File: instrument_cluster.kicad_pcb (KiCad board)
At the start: 2 copper layers, 144.8 x 45.7 mm, 76 parts, among them J1 Conn_02x16_Top_Bottom, J2 Conn_02x16_Top_Bottom, J3 USB mini-B SMD, J4 NOT_FITTED_SWD_Conn_01x04_Male, J5 54819-0572, J6 NOT_FITTED_SWD_Conn_01x04_Male, U1 LM2575S-5.0_NOPB, U10 74HC4050D, U11 TJA1040T, U12 TJA1040T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

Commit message: working with pcb design
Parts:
- D3, D5, D6: moved to B.Cu
- moved R18 98.0 mm to (150.5, 145.5)
- moved C29 97.7 mm to (146.0, 145.5)
- moved C28 97.5 mm to (142.0, 145.5)
- moved R17 97.4 mm to (154.0, 144.5)
- moved R20 94.6 mm to (154.9, 141.5), turned to 180 degrees
- moved R21 94.1 mm to (151.5, 141.5), turned to 180 degrees
- moved R22 93.2 mm to (146.5, 141.0), turned to 180 degrees
- moved R23 93.0 mm to (142.9, 141.0), turned to 180 degrees
- moved C5 87.6 mm to (151.0, 127.5), turned to 180 degrees
- moved U12 82.4 mm to (144.5, 135.5), turned to 90 degrees
- moved U11 82.0 mm to (153.5, 136.0), turned to 90 degrees
- moved C7 79.0 mm to (143.0, 127.0), turned to 270 degrees
- moved D6 78.9 mm to (168.0, 122.0), turned to 270 degrees
- moved C6 61.6 mm to (149.0, 100.0), turned to 180 degrees
- moved C8 47.1 mm to (143.0, 95.0)
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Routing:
- net GND: track 159.1 -> 287.4 mm, vias 2 -> 9
- net /MS_CAN_H: track 34.8 -> 145.8 mm
- net /MS_CAN_L: track 40.4 -> 148.0 mm
- net /HS_CAN_H: track 31.1 -> 138.4 mm, vias 0 -> 1
- net /HS_CAN_L: track 32.4 -> 137.2 mm, vias 0 -> 1
- net /+5V_B: track 0.00 -> 52.2 mm, vias 0 -> 3
- net /Module B (2can_filter+extra)/anti-theft_stm: track 4.32 -> 52.4 mm, vias 0 -> 2
- net /Module B (2can_filter+extra)/washer: track 4.41 -> 52.2 mm
- net /Module B (2can_filter+extra)/oil_pressure_level: track 7.69 -> 55.1 mm
- net /Module B (2can_filter+extra)/belt: track 10.9 -> 57.8 mm, vias 0 -> 2
- net /Module B (2can_filter+extra)/brake_fluid_level: track 4.07 -> 50.6 mm, vias 0 -> 2
- net /Module B (2can_filter+extra)/trip_comp: track 9.53 -> 55.9 mm, vias 0 -> 2
- net /Module B (2can_filter+extra)/engine_coolant: track 10.5 -> 55.2 mm
- net /Module B (2can_filter+extra)/parking_brakes: track 9.51 -> 53.9 mm, vias 0 -> 2
- net /Module B (2can_filter+extra)/pad_wear: track 4.31 -> 47.8 mm, vias 0 -> 2
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
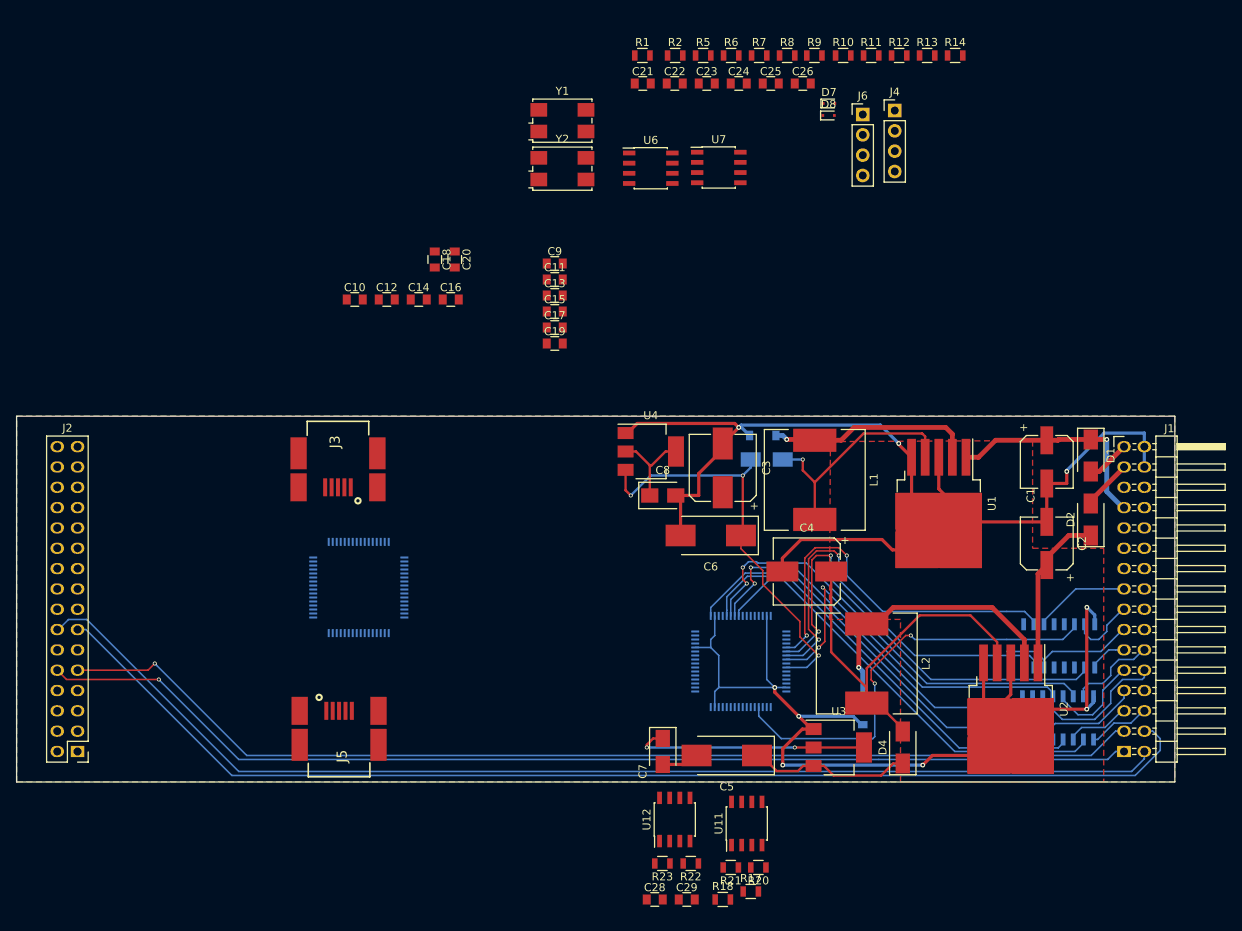
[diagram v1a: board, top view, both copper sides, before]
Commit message: redone shematic of power supply, fix usb_vbus and swd diods connections, change mcu capacitors connections
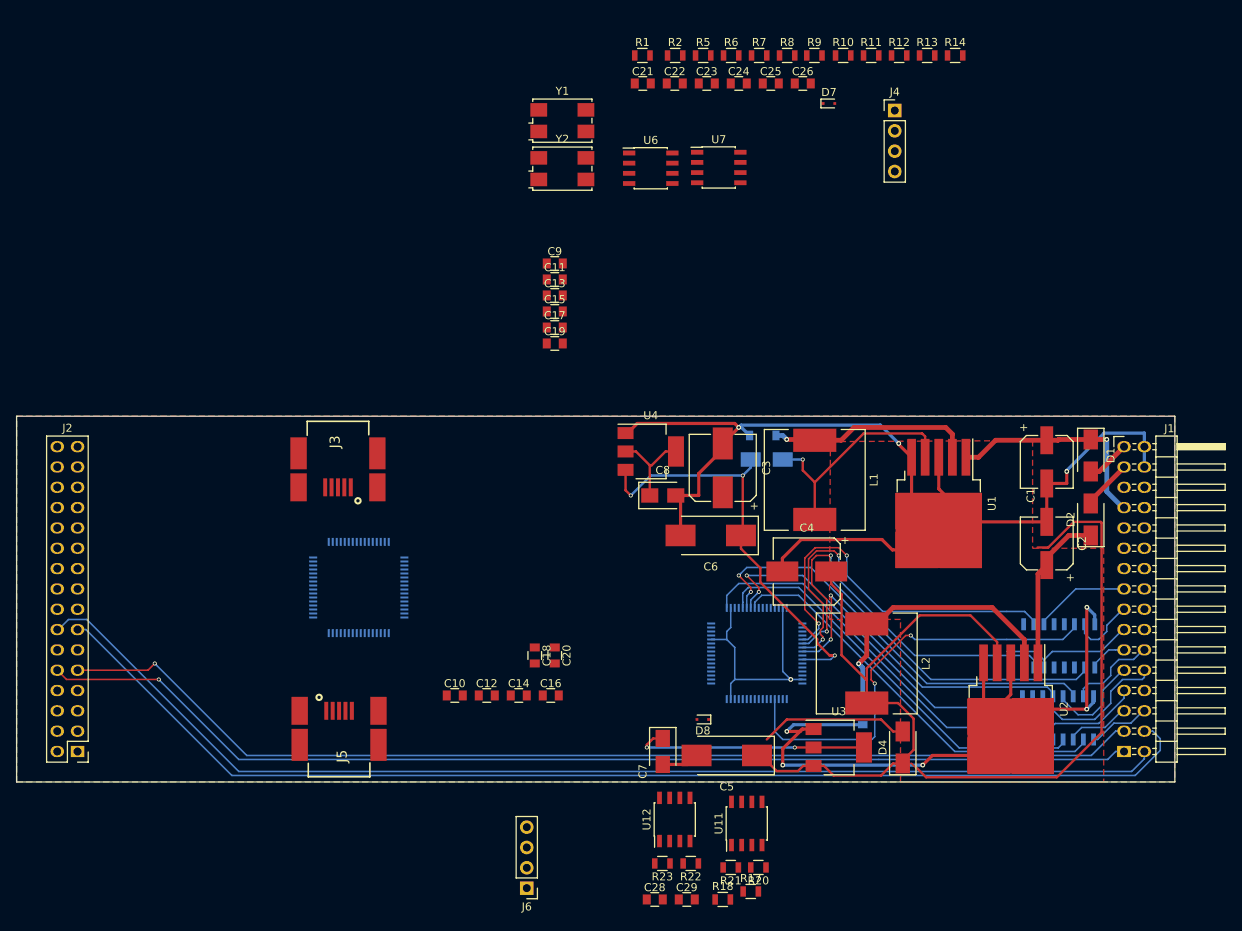
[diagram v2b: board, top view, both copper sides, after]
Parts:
- moved J6 105.4 mm to (126.0, 144.1), turned to 180 degrees
- moved D8 77.1 mm to (148.0, 123.0), turned to 180 degrees
- moved C10 51.1 mm to (117.0, 120.0)
- moved C12 51.1 mm to (121.0, 120.0)
- moved C14 51.1 mm to (125.0, 120.0)
- moved C16 51.1 mm to (129.0, 120.0)
- moved C18 51.1 mm to (127.0, 115.0)
- moved C20 51.1 mm to (129.5, 115.0)
- moved U9 2.24 mm to (154.8, 114.8)
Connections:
- net Net-(J4-Pad2) renamed /Module A (2can_filter)/SWCLK
- net Net-(J4-Pad3) renamed /Module A (2can_filter)/SWDIO
- net Net-(J6-Pad2) renamed /Module B (2can_filter+extra)/SWCLK
- net Net-(J6-Pad3) renamed /Module B (2can_filter+extra)/SWDIO
- C10 pad 1: /+3V3_B -> /+3V3_STM-B
- C11 pad 1: /+3V3_A -> /+3V3_STM-A
- C12 pad 1: /+3V3_B -> /+3V3_STM-B
- C13 pad 1: /+3V3_A -> /+3V3_STM-A
- C14 pad 1: /+3V3_B -> /+3V3_STM-B
- C15 pad 1: /+3V3_A -> /+3V3_STM-A
- C16 pad 1: /+3V3_B -> /+3V3_STM-B
- C17 pad 1: /+3V3_A -> /+3V3_STM-A
- C18 pad 1: /+3V3_B -> /+3V3_STM-B
- C19 pad 1: /+3V3_A -> /+3V3_STM-A
- C20 pad 1: /+3V3_B -> /+3V3_STM-B
- C3 pad 1: /power_supply/+5V_B_module -> /+5V_CAN-B
- C4 pad 1: /power_supply/+5V_A_module -> /+5V_CAN-A
- C5 pad 1: /+5V_A -> /+5V_CAN-A
- C6 pad 1: /+5V_B -> /+5V_CAN-B
- C7 pad 1: /+3V3_A -> Net-(C7-Pad1)
- C8 pad 1: /+3V3_B -> /+3V3_LSH-B
- C9 pad 1: /+3V3_A -> /+3V3_STM-A
- D3 pad 1: /+5V_B -> /+5V_CAN-B
- D3 pad 2: /power_supply/+5V_B_module -> /USB_Vbus-B
- D4 pad 1: /+5V_A -> /+5V_CAN-A
- D4 pad 2: /power_supply/+5V_A_module -> /USB_Vbus-A
- D7 pad 1: /+3V3_A -> /+3V3_STM-A
- D7 pad 2: /+3V3_A -> Net-(C7-Pad1)
- D8 pad 1: /+3V3_B -> /+3V3_STM-B
- D8 pad 2: /+3V3_B -> /+3V3_LSH-B
- J3 pad 1: /+5V_A -> /USB_Vbus-A
- J4 pad 4: /+3V3_A -> /+3V3_STM-A
- J5 pad 1: /+5V_B -> /USB_Vbus-B
- J6 pad 4: /+3V3_B -> /+3V3_STM-B
- L1 pad 2: /power_supply/+5V_B_module -> /+5V_CAN-B
- L2 pad 2: /power_supply/+5V_A_module -> /+5V_CAN-A
- U1 pad 4: /power_supply/+5V_B_module -> /+5V_CAN-B
- U10 pad 1: /+3V3_B -> /+3V3_LSH-B
- U11 pad 3: /+5V_B -> /+5V_CAN-B
- U12 pad 3: /+5V_B -> /+5V_CAN-B
- U2 pad 4: /power_supply/+5V_A_module -> /+5V_CAN-A
- U3 pad 2: /+3V3_A -> Net-(C7-Pad1)
- U3 pad 3: /+5V_A -> /+5V_CAN-A
- U4 pad 2: /+3V3_B -> /+3V3_LSH-B
- U4 pad 3: /+5V_B -> /+5V_CAN-B
- U5 pad 1: /+3V3_A -> /+3V3_STM-A
- U5 pad 13: /+3V3_A -> /+3V3_STM-A
- U5 pad 19: /+3V3_A -> /+3V3_STM-A
- U5 pad 32: /+3V3_A -> /+3V3_STM-A
- U5 pad 42: /+5V_A -> /USB_Vbus-A
- U5 pad 48: /+3V3_A -> /+3V3_STM-A
- U5 pad 64: /+3V3_A -> /+3V3_STM-A
- U6 pad 3: /+5V_A -> /+5V_CAN-A
- U7 pad 3: /+5V_A -> /+5V_CAN-A
- U8 pad 1: /+3V3_B -> /+3V3_LSH-B
- U9 pad 1: /+3V3_B -> /+3V3_STM-B
- U9 pad 13: /+3V3_B -> /+3V3_STM-B
- U9 pad 19: /+3V3_B -> /+3V3_STM-B
- U9 pad 32: /+3V3_B -> /+3V3_STM-B
- U9 pad 42: /+5V_B -> /USB_Vbus-B
- U9 pad 48: /+3V3_B -> /+3V3_STM-B
- U9 pad 64: /+3V3_B -> /+3V3_STM-B
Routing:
- net /+5V_CAN-A: track 0.00 -> 139.5 mm
- net /+5V_CAN-B: track 0.00 -> 76.7 mm, vias 0 -> 3
- net /+5V_B: track 52.2 -> 0.00 mm, vias 3 -> 0
- net /power_supply/+5V_A_module: track 51.9 -> 0.00 mm
- net Net-(C7-Pad1): track 0.00 -> 29.8 mm, vias 0 -> 2
- net /+3V3_A: track 29.8 -> 0.00 mm, vias 2 -> 0
- net /power_supply/+5V_B_module: track 29.7 -> 0.00 mm, vias 1 -> 0
- net /+5V_A: track 20.4 -> 0.00 mm
- net /USB_Vbus-A: track 0.00 -> 18.7 mm
- net /+3V3_LSH-B: track 0.00 -> 11.5 mm
- net /+3V3_B: track 11.5 -> 0.00 mm
- net /USB_Vbus-B: track 0.00 -> 6.05 mm, vias 0 -> 1
- net /Module B (2can_filter+extra)/illum_stm: track 47.3 -> 43.0 mm
- net /Module B (2can_filter+extra)/engine_coolant: track 55.2 -> 51.1 mm
- net GND: track 287.4 -> 283.5 mm
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
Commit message: reduce board edge, finish module B tracing
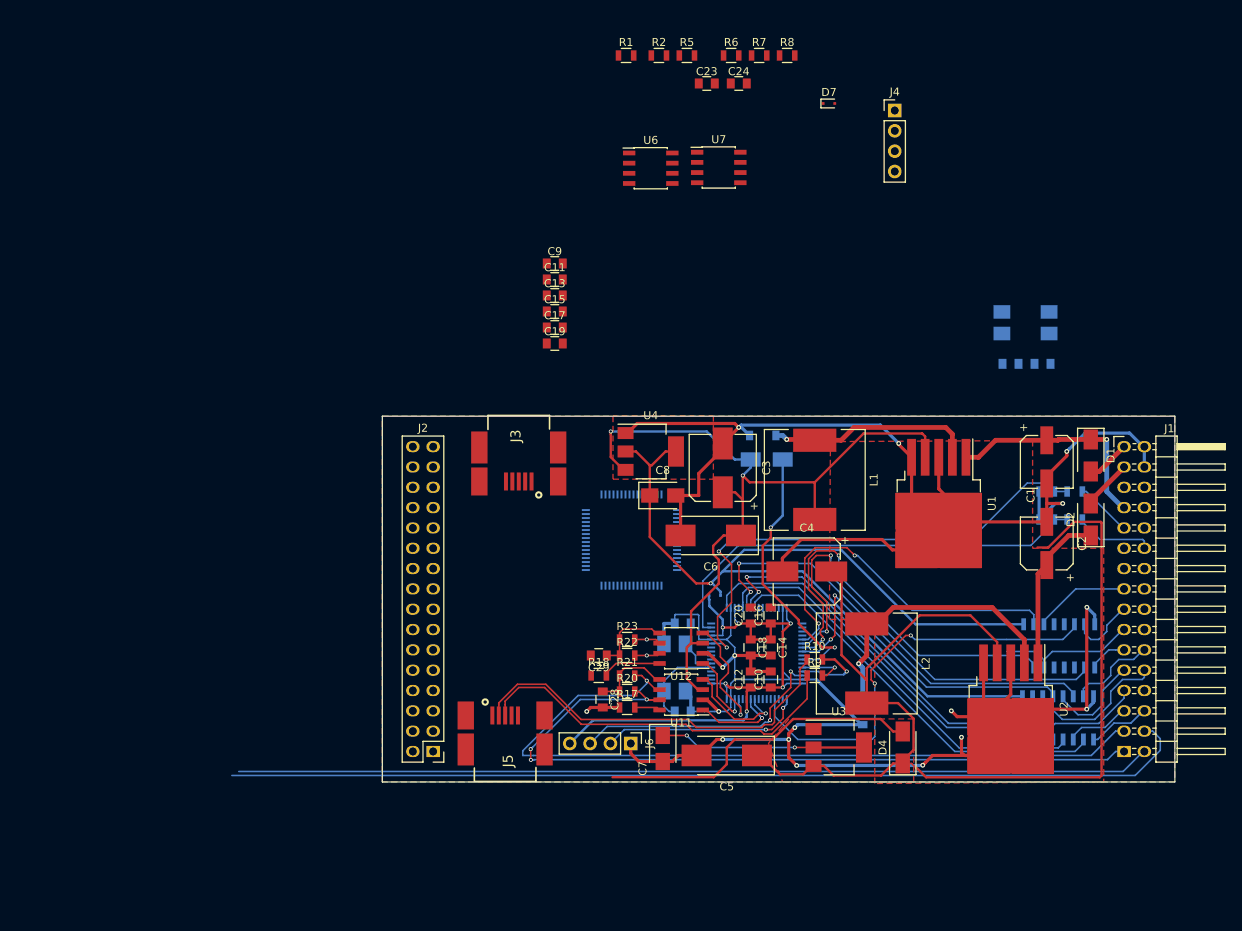
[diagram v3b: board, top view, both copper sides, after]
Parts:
- C21, C22, C25, C26, D8, R11, R12, R13, R14, Y1, Y2: moved to B.Cu
- moved C25 79.3 mm to (145.5, 122.0)
- moved R9 77.5 mm to (162.0, 117.5)
- moved R10 75.6 mm to (162.0, 115.5)
- moved C26 69.1 mm to (145.5, 111.0), turned to 180 degrees
- moved Y2 63.9 mm to (144.5, 116.5), turned to 90 degrees
- moved R11 63.3 mm to (194.5, 98.0)
- moved Y1 63.2 mm to (188.3, 73.4)
- moved R13 59.9 mm to (191.0, 98.0)
- moved R12 58.8 mm to (194.5, 94.5)
- moved C21 57.8 mm to (186.5, 78.5)
- moved C22 57.8 mm to (190.5, 78.5)
- moved R14 55.7 mm to (191.0, 94.5)
- moved J2 44.5 mm to (114.3, 88.9)
- moved C10 39.6 mm to (156.5, 118.0), turned to 90 degrees
- moved U5 34.6 mm to (139.1, 100.6), turned to 180 degrees
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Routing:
- net /+3V3_LSH-B: track 11.5 -> 117.5 mm, vias 0 -> 1
- net GND: track 283.5 -> 366.4 mm, vias 9 -> 17
- net /+3V3_STM-B: track 0.00 -> 76.3 mm, vias 0 -> 6
- net /Module B (2can_filter+extra)/stm_adc_2: track 0.00 -> 63.7 mm, vias 0 -> 2
- net /Module B (2can_filter+extra)/stm_adc_1: track 0.00 -> 55.8 mm
- net Net-(J5-Pad2): track 0.00 -> 49.1 mm
- net Net-(J5-Pad3): track 0.00 -> 47.4 mm
- net /HS_CAN_H: track 138.4 -> 98.2 mm, vias 1 -> 3
- net /HS_CAN_L: track 137.2 -> 100.2 mm
- net /Module B (2can_filter+extra)/SWDIO: track 0.00 -> 32.5 mm, vias 0 -> 2
- net /MS_CAN_H: track 145.8 -> 117.4 mm, vias 0 -> 1
- net /USB_Vbus-B: track 6.05 -> 33.8 mm, vias 1 -> 2
- net /Module B (2can_filter+extra)/SWCLK: track 0.00 -> 25.5 mm, vias 0 -> 2
- net /MS_CAN_L: track 148.0 -> 124.5 mm, vias 0 -> 1
- net /USB_Vbus-A: track 18.7 -> 41.2 mm
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- added copper zone on F.Cu, net /+3V3_LSH-B
- added copper zone on F.Cu, net Net-(C7-Pad1)
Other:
- board size 144.8 x 45.7 mm -> 99.1 x 45.7 mm

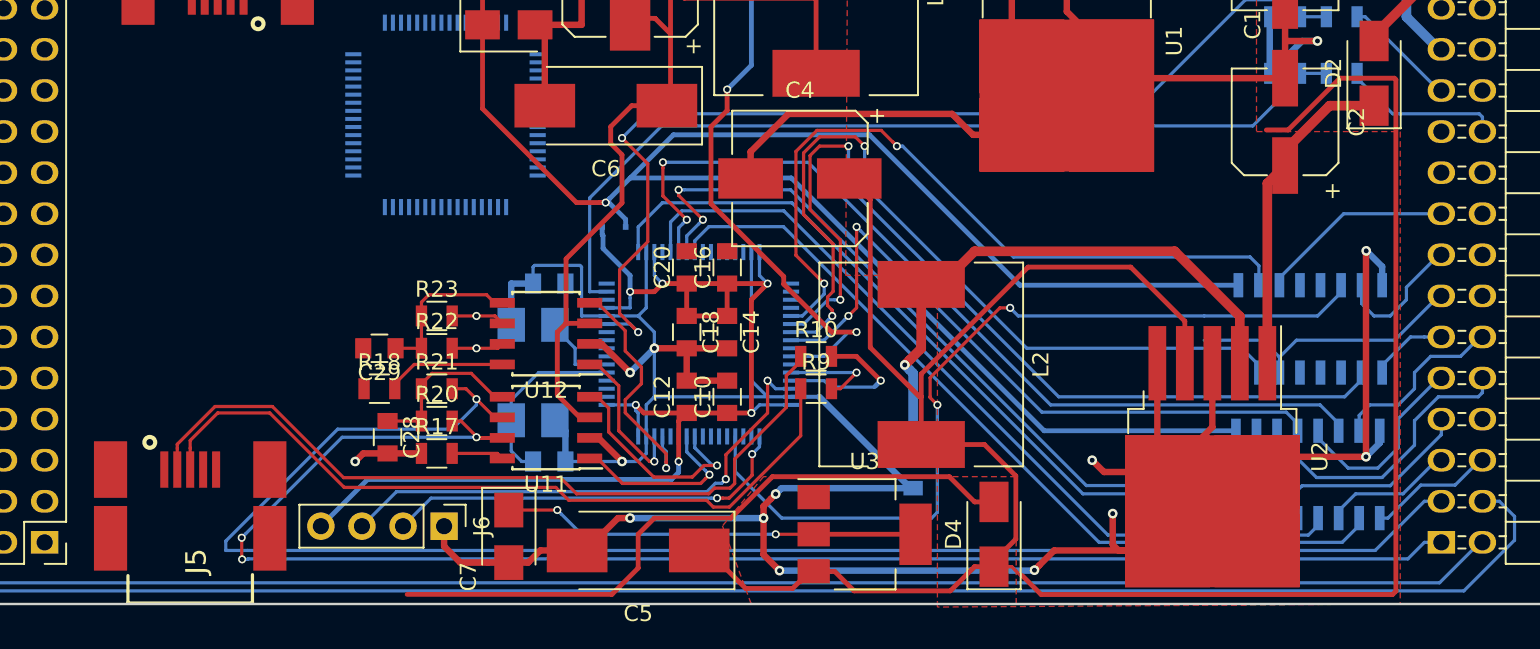
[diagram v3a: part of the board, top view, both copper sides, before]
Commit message: add transient voltage suppression diods on CAN
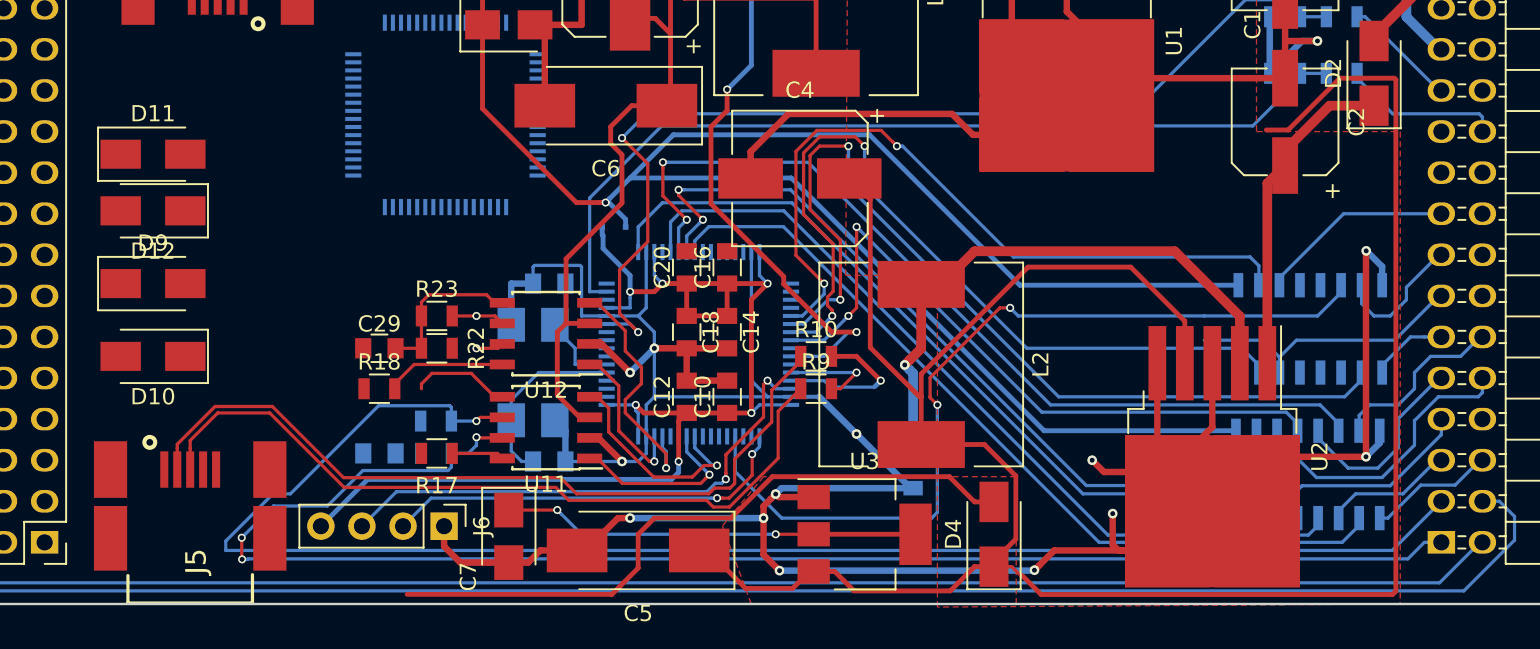
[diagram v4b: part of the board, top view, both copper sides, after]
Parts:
- added D10: SMAJ33CA-TR, Diodes_SMD:D_SMA, F.Cu at (121.0, 115.5)
- added D11: SMAJ33CA-TR, Diodes_SMD:D_SMA, F.Cu at (121.0, 103.0)
- added D12: SMAJ33CA-TR, Diodes_SMD:D_SMA, F.Cu at (121.0, 106.5)
- added D9: SMAJ33CA-TR, Diodes_SMD:D_SMA, F.Cu at (121.0, 111.0)
- C28, R20, R21: moved to B.Cu
- moved R20 2.00 mm to (138.5, 121.5), turned to 180 degrees
- moved R21 2.00 mm to (138.5, 119.5)
- moved C28 1.12 mm to (135.0, 121.5), turned to 180 degrees
- turned C29 to 0 degrees
- turned R22 to 180 degrees
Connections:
- C23 pad 1: Net-(C23-Pad1) -> GND
- C23 pad 2: GND -> Net-(C23-Pad2)
- C24 pad 1: Net-(C24-Pad1) -> GND
- C24 pad 2: GND -> Net-(C24-Pad2)
- C29 pad 1: Net-(C29-Pad1) -> GND
- C29 pad 2: GND -> Net-(C29-Pad2)
- R20 pad 1: Net-(C28-Pad1) -> /HS_CAN_H
- R20 pad 2: /HS_CAN_H -> Net-(C28-Pad1)
- R22 pad 1: Net-(C29-Pad1) -> /MS_CAN_H
- R22 pad 2: /MS_CAN_H -> Net-(C29-Pad2)
- R23 pad 1: Net-(C29-Pad1) -> Net-(C29-Pad2)
- R5 pad 1: Net-(C23-Pad1) -> Net-(C23-Pad2)
- R6 pad 1: Net-(C23-Pad1) -> Net-(C23-Pad2)
- R7 pad 1: Net-(C24-Pad1) -> /MS_CAN_H
- R7 pad 2: /MS_CAN_H -> Net-(C24-Pad2)
- R8 pad 1: Net-(C24-Pad1) -> Net-(C24-Pad2)
- U12 pad 5: Net-(C29-Pad1) -> Net-(C29-Pad2)
- U5 pad 57: Net-(U5-Pad57) -> /Module A (2can_filter)/CAN2_RX
- U5 pad 58: Net-(U5-Pad58) -> /Module A (2can_filter)/CAN2_TX
- U5 pad 61: Net-(U5-Pad61) -> /Module A (2can_filter)/CAN1_RX
- U5 pad 62: Net-(U5-Pad62) -> /Module A (2can_filter)/CAN1_TX
- U6 pad 1: Net-(U5-Pad58) -> /Module A (2can_filter)/CAN1_TX
- U6 pad 4: Net-(U5-Pad57) -> /Module A (2can_filter)/CAN1_RX
- U6 pad 5: Net-(C23-Pad1) -> Net-(C23-Pad2)
- U7 pad 1: Net-(U5-Pad62) -> /Module A (2can_filter)/CAN2_TX
- U7 pad 4: Net-(U5-Pad61) -> /Module A (2can_filter)/CAN2_RX
- U7 pad 5: Net-(C24-Pad1) -> Net-(C24-Pad2)
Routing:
- net Net-(C29-Pad2): track 0.00 -> 9.85 mm
- net Net-(C29-Pad1): track 9.85 -> 0.00 mm
- net Net-(C28-Pad1): track 10.3 -> 6.17 mm
- net /HS_CAN_H: track 98.2 -> 95.4 mm
- net GND: track 366.4 -> 364.5 mm
- net /HS_CAN_L: track 100.2 -> 98.6 mm
- net /MS_CAN_H: track 117.4 -> 115.9 mm

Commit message: work on module A
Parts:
- C29, R22, R23: moved to B.Cu
- moved J4 55.3 mm to (134.5, 87.5)
- moved U6 51.6 mm to (128.5, 104.0), turned to 180 degrees
- moved U7 49.4 mm to (128.5, 98.5), turned to 180 degrees
- moved Y1 44.9 mm to (149.5, 96.0), turned to 270 degrees
- moved C22 40.2 mm to (154.5, 96.5)
- moved C23 36.1 mm to (146.5, 79.5)
- moved C24 36.1 mm to (150.5, 79.5)
- moved D7 36.1 mm to (161.8, 82.0)
- moved R1 36.1 mm to (136.4, 76.0)
- moved R2 36.1 mm to (140.5, 76.0)
- moved R5 36.1 mm to (144.0, 76.0)
- moved R6 36.1 mm to (149.6, 76.0)
- moved R7 36.1 mm to (153.1, 76.0)
- moved R8 36.1 mm to (156.6, 76.0)
- moved C21 35.7 mm to (154.5, 94.5)
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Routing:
- net /VBATT: track 5.44 -> 151.1 mm
- net /MS_CAN_L: track 124.5 -> 81.5 mm
- net /MS_CAN_H: track 115.9 -> 74.9 mm
- net GND: track 364.5 -> 402.9 mm, vias 17 -> 20
- net /HS_CAN_L: track 98.6 -> 72.9 mm
- net /HS_CAN_H: track 95.4 -> 73.6 mm, vias 3 -> 1
- net Net-(C21-Pad1): track 0.00 -> 11.4 mm
- net Net-(C22-Pad1): track 0.00 -> 8.15 mm
- net (no net): track 0.00 -> 4.35 mm
- net Net-(R18-Pad2): track 7.45 -> 3.24 mm
- net /+3V3_STM-B: track 76.3 -> 72.2 mm
- net Net-(C28-Pad1): track 6.17 -> 9.20 mm, vias 0 -> 1
- net /+5V_CAN-B: track 97.2 -> 99.9 mm
- net /Module B (2can_filter+extra)/stm_adc_2: track 63.7 -> 61.2 mm
- net /+3V3_LSH-B: track 117.5 -> 115.3 mm
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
